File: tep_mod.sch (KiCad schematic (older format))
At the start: 3 parts

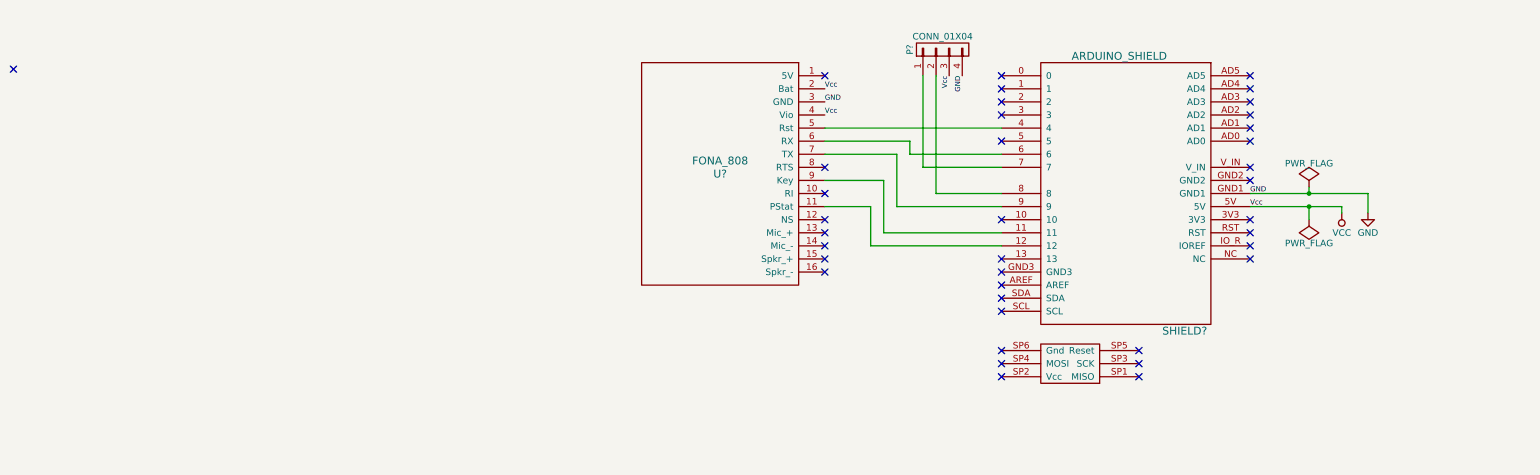
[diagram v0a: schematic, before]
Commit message: Pin assignment changes
Freeing SPI bus for SD card use. Adding ICSP breakout on top. RTS pin
assigned. Other small changes and tidying up.
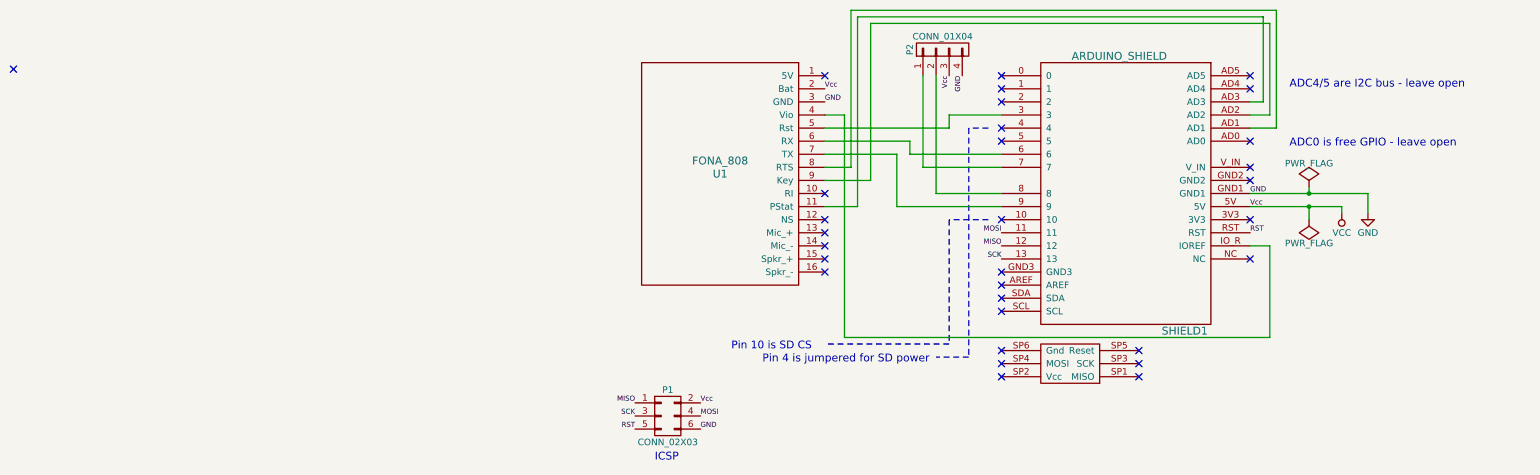
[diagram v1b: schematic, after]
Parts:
- added P1: CONN_02X03, symbol CONN_02X03
- gave numbers to parts that had none: 3
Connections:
- net GND: now also P1.6 (P6)
- net VCC: now also P1.2 (P2); no longer U1.4 (Vio)
- net at U1.11 (PStat): now also SHIELD1.AD3; no longer SHIELD1.12
- net at U1.5 (Rst): now also SHIELD1.3; no longer SHIELD1.4
- net at U1.8 (RTS): now also SHIELD1.AD1
- net at U1.9 (Key): now also SHIELD1.AD2; no longer SHIELD1.11
- net SCK: now reaches SHIELD1.13
- net SCK: now also P1.3 (P3)
- net at SHIELD1.IO_R (IOREF): now also U1.4 (Vio)
- net RST: now reaches SHIELD1.RST
- net RST: now also P1.5 (P5)
- new net MISO: P1.1 (P1), SHIELD1.12
- new net MOSI: P1.4 (P4), SHIELD1.11
- no-connect marks 38 -> 31
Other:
- note added: "ADC0 is free GPIO - leave open\n"
- note added: "ADC4/5 are I2C bus - leave open"
- note added: "ICSP"
- note added: "Pin 10 is SD CS"
- note added: "Pin 4 is jumpered for SD power"
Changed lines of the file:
@@
 LIBS:contrib
 LIBS:valves
+LIBS:tep_mod-cache
 EELAYER 25 0
 EELAYER END
@@
 Title "Extending Tepmachcha "
 Date "2017-04-07"
-Rev "0.1"
+Rev "0.2"
 Comp "Theorent / STEM Phnom Penh"
 Comment1 ""
@@
 $EndDescr
 $Comp
-L FONA_808 U?
+L FONA_808 U1
 U 1 1 58E70BC9
 P 3550 3750
-F 0 "U?" H 3550 3700 60  0000 C CNN
+F 0 "U1" H 3550 3700 60  0000 C CNN
 F 1 "FONA_808" H 3550 3800 60  0000 C CNN
 F 2 "DAI_Maker_Lab_footprints:FONA_808" H 3550 3750 60  0001 C CNN
@@
 	1    0    0    -1
 $EndComp
-$Comp
-L ARDUINO_SHIELD SHIELD?
-U 1 1 58E70BCA
-P 6650 3850
-F 0 "SHIELD?" H 6200 5000 60  0000 C CNN
-F 1 "ARDUINO_SHIELD" H 6700 2900 60  0000 C CNN
-F 2 "freetronics_footprints:ARDUINO_SHIELD" H 6650 3650 50  0001 C CNN
-F 3 "" H 6650 3850 60  0000 C CNN
-	1    6650 3850
-	-1   0    0    1
-$EndComp
-Wire Wire Line
-	4350 3450 5700 3450
 Wire Wire Line
 	4350 3550 5000 3550
@@
 Wire Wire Line
 	4900 4050 5700 4050
-Wire Wire Line
-	4350 3850 4800 3850
-Wire Wire Line
-	4800 3850 4800 4250
-Wire Wire Line
-	4800 4250 5700 4250
-Wire Wire Line
-	4350 4050 4700 4050
-Wire Wire Line
-	4700 4050 4700 4350
-Wire Wire Line
-	4700 4350 5700 4350
 Text Label 7600 3950 0    39   ~ 0
 GND
@@
 Vcc
 $Comp
-L GND #PWR?
+L GND #PWR01
 U 1 1 58E70BCB
 P 8500 4100
-F 0 "#PWR?" H 8500 3850 50  0001 C CNN
+F 0 "#PWR01" H 8500 3850 50  0001 C CNN
 F 1 "GND" H 8500 3950 50  0000 C CNN
 F 2 "" H 8500 4100 50  0000 C CNN
@@
 $EndComp
 $Comp
-L VCC #PWR?
+L VCC #PWR02
 U 1 1 58E70BCC
 P 8300 4100
-F 0 "#PWR?" H 8300 3950 50  0001 C CNN
+F 0 "#PWR02" H 8300 3950 50  0001 C CNN
 F 1 "VCC" H 8300 4250 50  0000 C CNN
 F 2 "" H 8300 4100 50  0000 C CNN
@@
 	8300 4050 7600 4050
 $Comp
-L PWR_FLAG #FLG?
+L PWR_FLAG #FLG03
 U 1 1 58E70BCD
 P 8050 3900
-F 0 "#FLG?" H 8050 3995 50  0001 C CNN
+F 0 "#FLG03" H 8050 3995 50  0001 C CNN
 F 1 "PWR_FLAG" H 8050 4080 50  0000 C CNN
 F 2 "" H 8050 3900 50  0000 C CNN
@@
 $EndComp
 $Comp
-L PWR_FLAG #FLG?
+L PWR_FLAG #FLG04
 U 1 1 58E70BCE
 P 8050 4150
-F 0 "#FLG?" H 8050 4245 50  0001 C CNN
+F 0 "#FLG04" H 8050 4245 50  0001 C CNN
 F 1 "PWR_FLAG" H 8050 4330 50  0000 C CNN
 F 2 "" H 8050 4150 50  0000 C CNN
@@
 Text Label 4350 3250 0    39   ~ 0
 GND
-Text Label 4350 3350 0    39   ~ 0
-Vcc
 NoConn ~ 4350 3050
-NoConn ~ 4350 3750
 NoConn ~ 4350 3950
 NoConn ~ 4350 4150
@@
 NoConn ~ -1850 3000
 $Comp
-L CONN_01X04 P?
+L CONN_01X04 P2
 U 1 1 58E70BCF
 P 5250 2850
-F 0 "P?" H 5250 3100 50  0000 C CNN
+F 0 "P2" H 5250 3100 50  0000 C CNN
 F 1 "CONN_01X04" V 5350 2850 50  0000 C CNN
 F 2 "DAI_Maker_Lab_footprints:Grove_straight" H 5250 2850 50  0001 C CNN
@@
 NoConn ~ 5700 3150
 NoConn ~ 5700 3250
-NoConn ~ 5700 3350
 NoConn ~ 5700 3550
 NoConn ~ 5700 4150
-NoConn ~ 5700 4450
-NoConn ~ 5700 4550
-NoConn ~ 5700 4650
 NoConn ~ 5700 4750
 NoConn ~ 5700 4850
@@
 NoConn ~ 6750 5350
 NoConn ~ 7600 4450
-NoConn ~ 7600 4350
-NoConn ~ 7600 4250
 NoConn ~ 7600 4150
 NoConn ~ 7600 3850
 NoConn ~ 7600 3750
 NoConn ~ 7600 3550
-NoConn ~ 7600 3450
-NoConn ~ 7600 3350
-NoConn ~ 7600 3250
 NoConn ~ 7600 3150
 NoConn ~ 7600 3050
+$Comp
+L ARDUINO_SHIELD SHIELD1
+U 1 1 58E70BCA
+P 6650 3850
+F 0 "SHIELD1" H 6200 5000 60  0000 C CNN
+F 1 "ARDUINO_SHIELD" H 6700 2900 60  0000 C CNN
+F 2 "freetronics_footprints:ARDUINO_SHIELD" H 6650 3650 50  0001 C CNN
+F 3 "" H 6650 3850 60  0000 C CNN
+	1    6650 3850
+	-1   0    0    1
+$EndComp
+Wire Wire Line
+	4350 3450 5300 3450
+Wire Wire Line
+	5300 3450 5300 3350
+Wire Wire Line
+	5300 3350 5700 3350
+NoConn ~ 5700 3450
+Wire Wire Line
+	4350 3850 4700 3850
+Wire Wire Line
+	4700 3850 4700 2650
+Wire Wire Line
+	4700 2650 7750 2650
+Wire Wire Line
+	7750 2650 7750 3350
+Wire Wire Line
+	7750 3350 7600 3350
+Wire Wire Line
+	4350 4050 4600 4050
+Wire Wire Line
+	4600 4050 4600 2600
+Wire Wire Line
+	4600 2600 7700 2600
+Wire Wire Line
+	7700 2600 7700 3250
+Wire Wire Line
+	7700 3250 7600 3250
+Wire Wire Line
+	4350 3750 4550 3750
+Wire Wire Line
+	4550 3750 4550 2550
+Wire Wire Line
+	4550 2550 7800 2550
+Wire Wire Line
+	7800 2550 7800 3450
+Wire Wire Line
+	7800 3450 7600 3450
+Wire Wire Line
+	4350 3350 4500 3350
+Wire Wire Line
+	4500 3350 4500 5050
+Wire Wire Line
+	4500 5050 7750 5050
+Wire Wire Line
+	7750 5050 7750 4350
+Wire Wire Line
+	7750 4350 7600 4350
+Text Notes 7900 3150 0    60   ~ 0
+ADC4/5 are I2C bus - leave open
+Text Notes 7900 3600 0    60   ~ 0
+ADC0 is free GPIO - leave open\n
+Wire Notes Line
+	5600 3450 5450 3450
+Wire Notes Line
+	5450 3450 5450 5200
+Wire Notes Line
+	5450 5200 5200 5200
+Text Notes 5150 5250 2    60   ~ 0
+Pin 4 is jumpered for SD power
+$Comp
+L CONN_02X03 P1
+U 1 1 58E7311B
+P 3150 5650
+F 0 "P1" H 3150 5850 50  0000 C CNN
+F 1 "CONN_02X03" H 3150 5450 50  0000 C CNN
+F 2 "" H 3150 4450 50  0000 C CNN
+F 3 "" H 3150 4450 50  0000 C CNN
+	1    3150 5650
+	1    0    0    -1
+$EndComp
+Text Notes 3050 6000 0    60   ~ 0
+ICSP
+Text Label 2900 5550 2    39   ~ 0
+MISO
+Text Label 2900 5650 2    39   ~ 0
+SCK
+Text Label 2900 5750 2    39   ~ 0
+RST
+Text Label 3400 5550 0    39   ~ 0
+Vcc
+Text Label 3400 5650 0    39   ~ 0
+MOSI
+Text Label 3400 5750 0    39   ~ 0
+GND
+Text Label 7600 4250 0    39   ~ 0
+RST
+Text Label 5700 4450 2    39   ~ 0
+SCK
+NoConn ~ 5700 4650
+NoConn ~ 5700 4550
+Text Label 5700 4350 2    39   ~ 0
+MISO
+Text Label 5700 4250 2    39   ~ 0
+MOSI
+Wire Notes Line
+	5600 4150 5300 4150
+Wire Notes Line
+	5300 4150 5300 5100
+Wire Notes Line
+	5300 5100 4350 5100
+Text Notes 4250 5150 2    59   ~ 0
+Pin 10 is SD CS
 $EndSCHEMATC

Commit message: v 0.1 board files
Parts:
- P1: footprint (none) -> Pin_Headers:Pin_Header_Straight_2x03
- P2: footprint DAI_Maker_Lab_footprints:Grove_straight -> Connectors:Grove_1x04
- U1: footprint DAI_Maker_Lab_footprints:FONA_808 -> freetronics_footprints:Adafruit_FONA_808_Theorent
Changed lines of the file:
@@
 F 0 "U1" H 3550 3700 60  0000 C CNN
 F 1 "FONA_808" H 3550 3800 60  0000 C CNN
-F 2 "DAI_Maker_Lab_footprints:FONA_808" H 3550 3750 60  0001 C CNN
+F 2 "freetronics_footprints:Adafruit_FONA_808_Theorent" H 3550 3750 60  0001 C CNN
 F 3 "" H 3550 3750 60  0000 C CNN
 	1    3550 3750
@@
 F 0 "P2" H 5250 3100 50  0000 C CNN
 F 1 "CONN_01X04" V 5350 2850 50  0000 C CNN
-F 2 "DAI_Maker_Lab_footprints:Grove_straight" H 5250 2850 50  0001 C CNN
+F 2 "Connectors:Grove_1x04" H 5250 2850 50  0001 C CNN
 F 3 "" H 5250 2850 50  0000 C CNN
 	1    5250 2850
@@
 F 0 "P1" H 3150 5850 50  0000 C CNN
 F 1 "CONN_02X03" H 3150 5450 50  0000 C CNN
-F 2 "" H 3150 4450 50  0000 C CNN
+F 2 "Pin_Headers:Pin_Header_Straight_2x03" H 3150 4450 50  0001 C CNN
 F 3 "" H 3150 4450 50  0000 C CNN
 	1    3150 5650
